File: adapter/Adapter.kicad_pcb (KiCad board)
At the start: 4 copper layers, 45.5 x 50 mm, 58 parts, among them J1 USB_B_Micro, J2 2040210-1, J3 USB_C_Receptacle, J4 Conn_01x05_Male, J5 Conn_01x03_Male, Q1 IRLML2244TRPBF, SW1 RESET, SW2 BOOT, U1 SN75DP119RGYT, U2 LD1117S33TR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

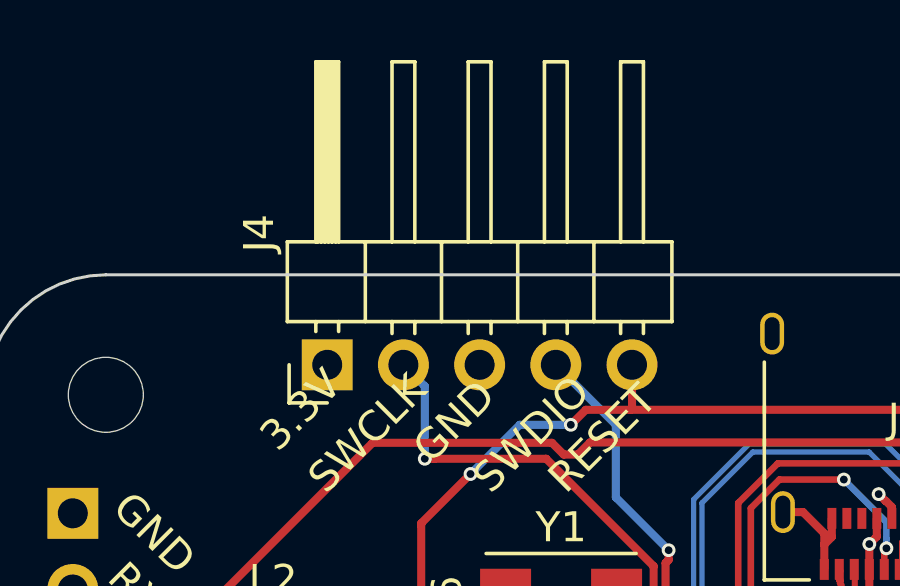
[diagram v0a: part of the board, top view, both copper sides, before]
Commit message: remove silkscreen from pin header footprints
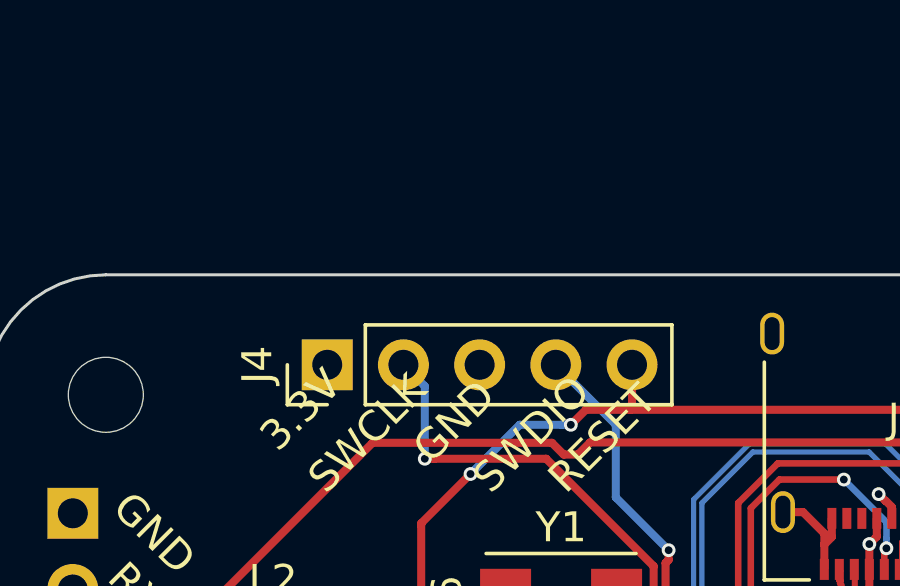
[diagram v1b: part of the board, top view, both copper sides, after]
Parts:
- J4: footprint Connector_PinHeader_2.54mm:PinHeader_1x05_P2.54mm_Horizontal -> Connector_PinHeader_2.54mm:PinHeader_1x05_P2.54mm_Vertical
- J5: footprint Connector_PinHeader_2.54mm:PinHeader_1x03_P2.54mm_Horizontal -> Connector_PinHeader_2.54mm:PinHeader_1x03_P2.54mm_Vertical

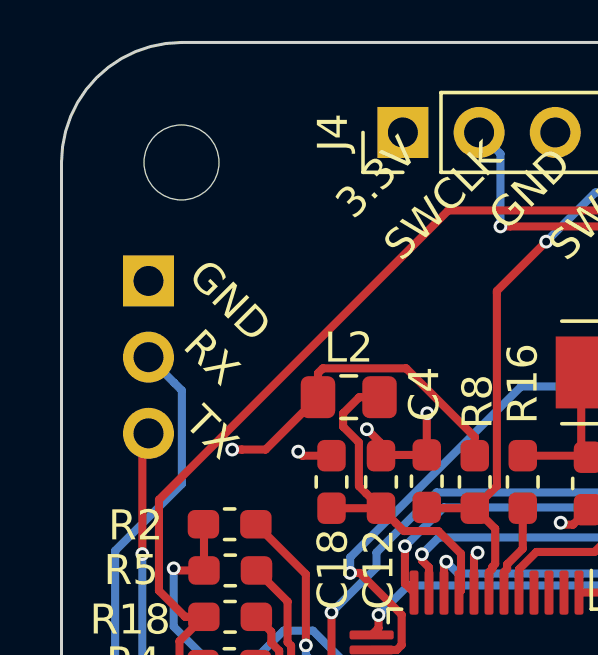
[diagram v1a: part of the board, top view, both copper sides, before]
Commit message: no silkscreen at bottom
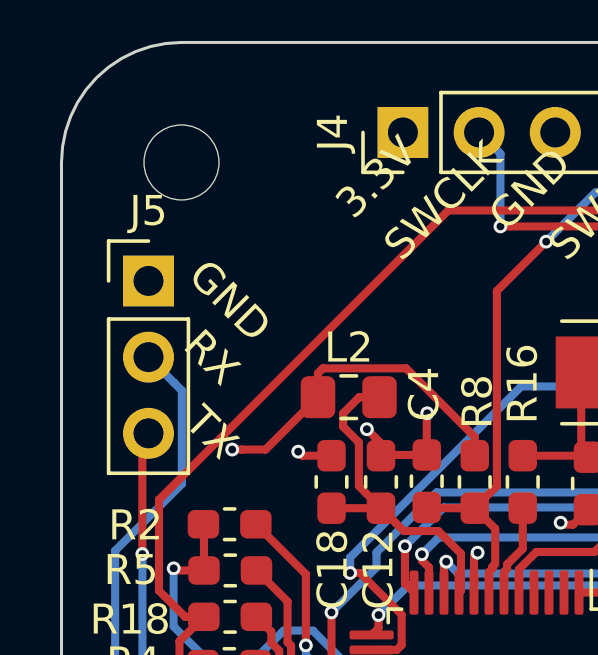
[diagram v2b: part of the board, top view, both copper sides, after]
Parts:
- J5: moved to F.Cu
- turned J5 to 0 degrees
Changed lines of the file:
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@@
     (add_net /D-)
   )
-  (module Connector_PinHeader_2.54mm:PinHeader_1x03_P2.54mm_Vertical (layer B.Cu)
-    (at 28.4 41.95 180)
+  (module Connector_PinHeader_2.54mm:PinHeader_1x03_P2.54mm_Vertical (layer F.Cu)
+    (at 28.4 41.95)
     (descr "Through hole straight pin header, 1x03, 2.54mm pitch, single row")
     (tags "Through hole pin header THT 1x03 2.54mm single row")
-    (fp_text reference J5 (at 0 2.33 180) (layer B.SilkS)
-      (effects (font (size 1 1) (thickness 0.15)) (justify mirror))
+    (fp_text reference J5 (at 0 -2.33) (layer F.SilkS)
+      (effects (font (size 1 1) (thickness 0.15)))
     )
-    (fp_text value Conn_01x03_Male (at 0 -7.41 180) (layer B.Fab)
-      (effects (font (size 1 1) (thickness 0.15)) (justify mirror))
+    (fp_text value Conn_01x03_Male (at 0 7.41) (layer F.Fab)
+      (effects (font (size 1 1) (thickness 0.15)))
     )
-    (fp_text user %R (at 0 -2.54 90) (layer B.Fab)
-      (effects (font (size 1 1) (thickness 0.15)) (justify mirror))
+    (fp_text user %R (at 0 2.54 90) (layer F.Fab)
+      (effects (font (size 1 1) (thickness 0.15)))
     )
-    (fp_line (start 1.8 1.8) (end -1.8 1.8) (layer B.CrtYd) (width 0.05))
-    (fp_line (start 1.8 -6.85) (end 1.8 1.8) (layer B.CrtYd) (width 0.05))
-    (fp_line (start -1.8 -6.85) (end 1.8 -6.85) (layer B.CrtYd) (width 0.05))
-    (fp_line (start -1.8 1.8) (end -1.8 -6.85) (layer B.CrtYd) (width 0.05))
-    (fp_line (start -1.33 1.33) (end 0 1.33) (layer B.SilkS) (width 0.12))
-    (fp_line (start -1.33 0) (end -1.33 1.33) (layer B.SilkS) (width 0.12))
-    (fp_line (start -1.33 -1.27) (end 1.33 -1.27) (layer B.SilkS) (width 0.12))
-    (fp_line (start 1.33 -1.27) (end 1.33 -6.41) (layer B.SilkS) (width 0.12))
-    (fp_line (start -1.33 -1.27) (end -1.33 -6.41) (layer B.SilkS) (width 0.12))
-    (fp_line (start -1.33 -6.41) (end 1.33 -6.41) (layer B.SilkS) (width 0.12))
-    (fp_line (start -1.27 0.635) (end -0.635 1.27) (layer B.Fab) (width 0.1))
-    (fp_line (start -1.27 -6.35) (end -1.27 0.635) (layer B.Fab) (width 0.1))
-    (fp_line (start 1.27 -6.35) (end -1.27 -6.35) (layer B.Fab) (width 0.1))
-    (fp_line (start 1.27 1.27) (end 1.27 -6.35) (layer B.Fab) (width 0.1))
-    (fp_line (start -0.635 1.27) (end 1.27 1.27) (layer B.Fab) (width 0.1))
-    (pad 3 thru_hole oval (at 0 -5.08 180) (size 1.7 1.7) (drill 1) (layers *.Cu *.Mask)
+    (fp_line (start 1.8 -1.8) (end -1.8 -1.8) (layer F.CrtYd) (width 0.05))
+    (fp_line (start 1.8 6.85) (end 1.8 -1.8) (layer F.CrtYd) (width 0.05))
+    (fp_line (start -1.8 6.85) (end 1.8 6.85) (layer F.CrtYd) (width 0.05))
+    (fp_line (start -1.8 -1.8) (end -1.8 6.85) (layer F.CrtYd) (width 0.05))
+    (fp_line (start -1.33 -1.33) (end 0 -1.33) (layer F.SilkS) (width 0.12))
+    (fp_line (start -1.33 0) (end -1.33 -1.33) (layer F.SilkS) (width 0.12))
+    (fp_line (start -1.33 1.27) (end 1.33 1.27) (layer F.SilkS) (width 0.12))
+    (fp_line (start 1.33 1.27) (end 1.33 6.41) (layer F.SilkS) (width 0.12))
+    (fp_line (start -1.33 1.27) (end -1.33 6.41) (layer F.SilkS) (width 0.12))
+    (fp_line (start -1.33 6.41) (end 1.33 6.41) (layer F.SilkS) (width 0.12))
+    (fp_line (start -1.27 -0.635) (end -0.635 -1.27) (layer F.Fab) (width 0.1))
+    (fp_line (start -1.27 6.35) (end -1.27 -0.635) (layer F.Fab) (width 0.1))
+    (fp_line (start 1.27 6.35) (end -1.27 6.35) (layer F.Fab) (width 0.1))
+    (fp_line (start 1.27 -1.27) (end 1.27 6.35) (layer F.Fab) (width 0.1))
+    (fp_line (start -0.635 -1.27) (end 1.27 -1.27) (layer F.Fab) (width 0.1))
+    (pad 3 thru_hole oval (at 0 5.08) (size 1.7 1.7) (drill 1) (layers *.Cu *.Mask)
       (net 58 /UART_TX))
-    (pad 2 thru_hole oval (at 0 -2.54 180) (size 1.7 1.7) (drill 1) (layers *.Cu *.Mask)
+    (pad 2 thru_hole oval (at 0 2.54) (size 1.7 1.7) (drill 1) (layers *.Cu *.Mask)
       (net 59 /UART_RX))
-    (pad 1 thru_hole rect (at 0 0 180) (size 1.7 1.7) (drill 1) (layers *.Cu *.Mask)
+    (pad 1 thru_hole rect (at 0 0) (size 1.7 1.7) (drill 1) (layers *.Cu *.Mask)
       (net 3 GND))
     (model ${KISYS3DMOD}/Connector_PinHeader_2.54mm.3dshapes/PinHeader_1x03_P2.54mm_Vertical.wrl

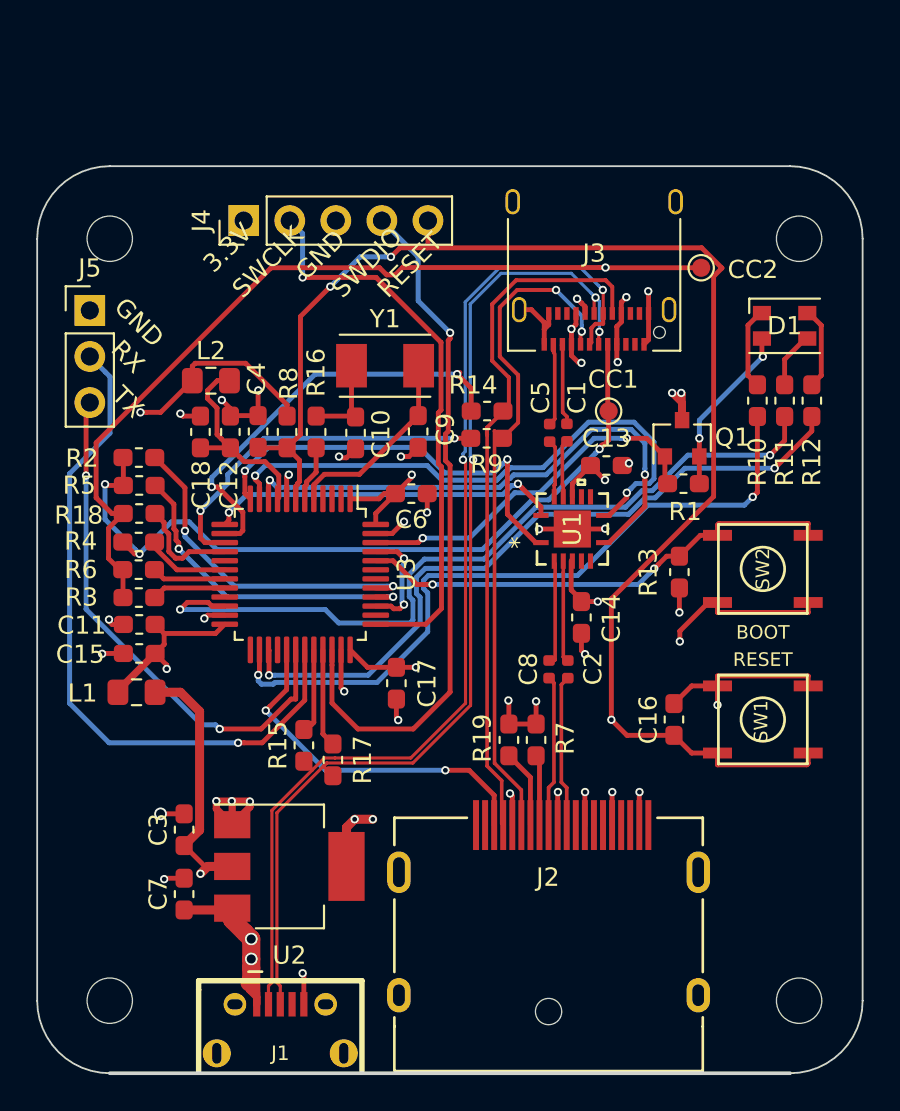
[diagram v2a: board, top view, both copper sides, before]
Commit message: fix distance between DP and µUSB connector
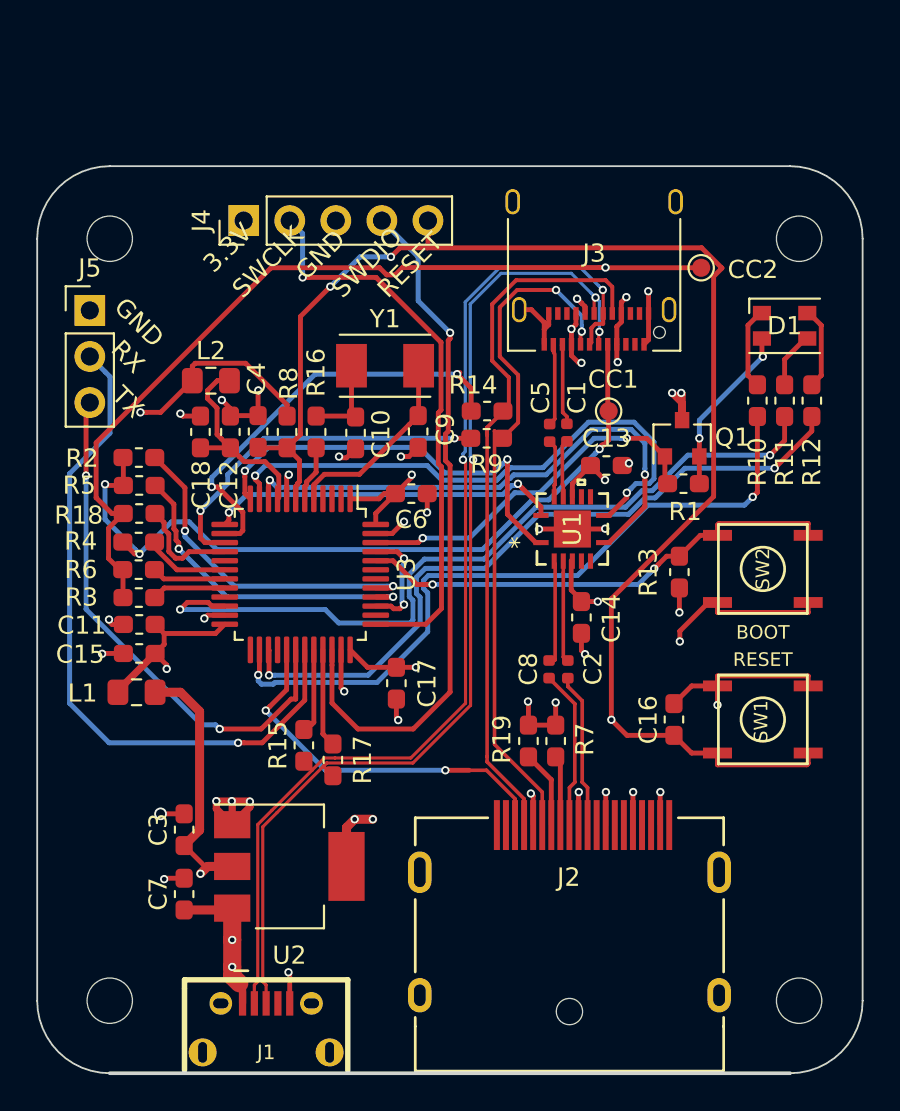
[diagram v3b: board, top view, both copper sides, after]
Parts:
- moved J2 1.15 mm to (54.8, 72.9)
- moved R19 1.08 mm to (52.6, 65.7)
- moved R7 1.08 mm to (54.1, 65.7)
- moved J1 0.78 mm to (38.1, 82.8)
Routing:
- net VBUS: track 19.2 -> 17.5 mm
- net /HPD: track 20.0 -> 21.0 mm
